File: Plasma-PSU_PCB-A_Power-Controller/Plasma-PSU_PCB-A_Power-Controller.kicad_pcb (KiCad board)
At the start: 2 copper layers, 160 x 100 mm, 98 parts, among them J201 PWR_FWD, J202 PWM_FWD, J203 Molex Mini-fit Jr. 39-28-1243, J204 Molex Mini-fit Jr. 39-28-1083, J205 Molex Mini-fit Jr. 39-28-1083, J206 Pinheader Controls, J207 ENBL_FWD, J301 Arduino_Pinout_01-15, J302 SPI, J303 UART, J304 I2C, J305 Arduino_Pinout_16-30, J501 Probe_Vin, J502 Probe_Iin, J503 JP_RUN, J504 Probe_Iout, J505 Probe_Vout, J506 Probe_DAC_A, J507 Probe_DAC_B, J508 OPAMP_Vout, J509 OPAMP_Iout, Q201 BC818, Q202 BC818, Q203 BT169B, Q204 BC808, Q501 NVTFS6H850NL, Q502 NVTFS6H850NL, U201 STM6600, U501 MCP602, U502 MCP602, U503 LTC3786, U504 MCP4822

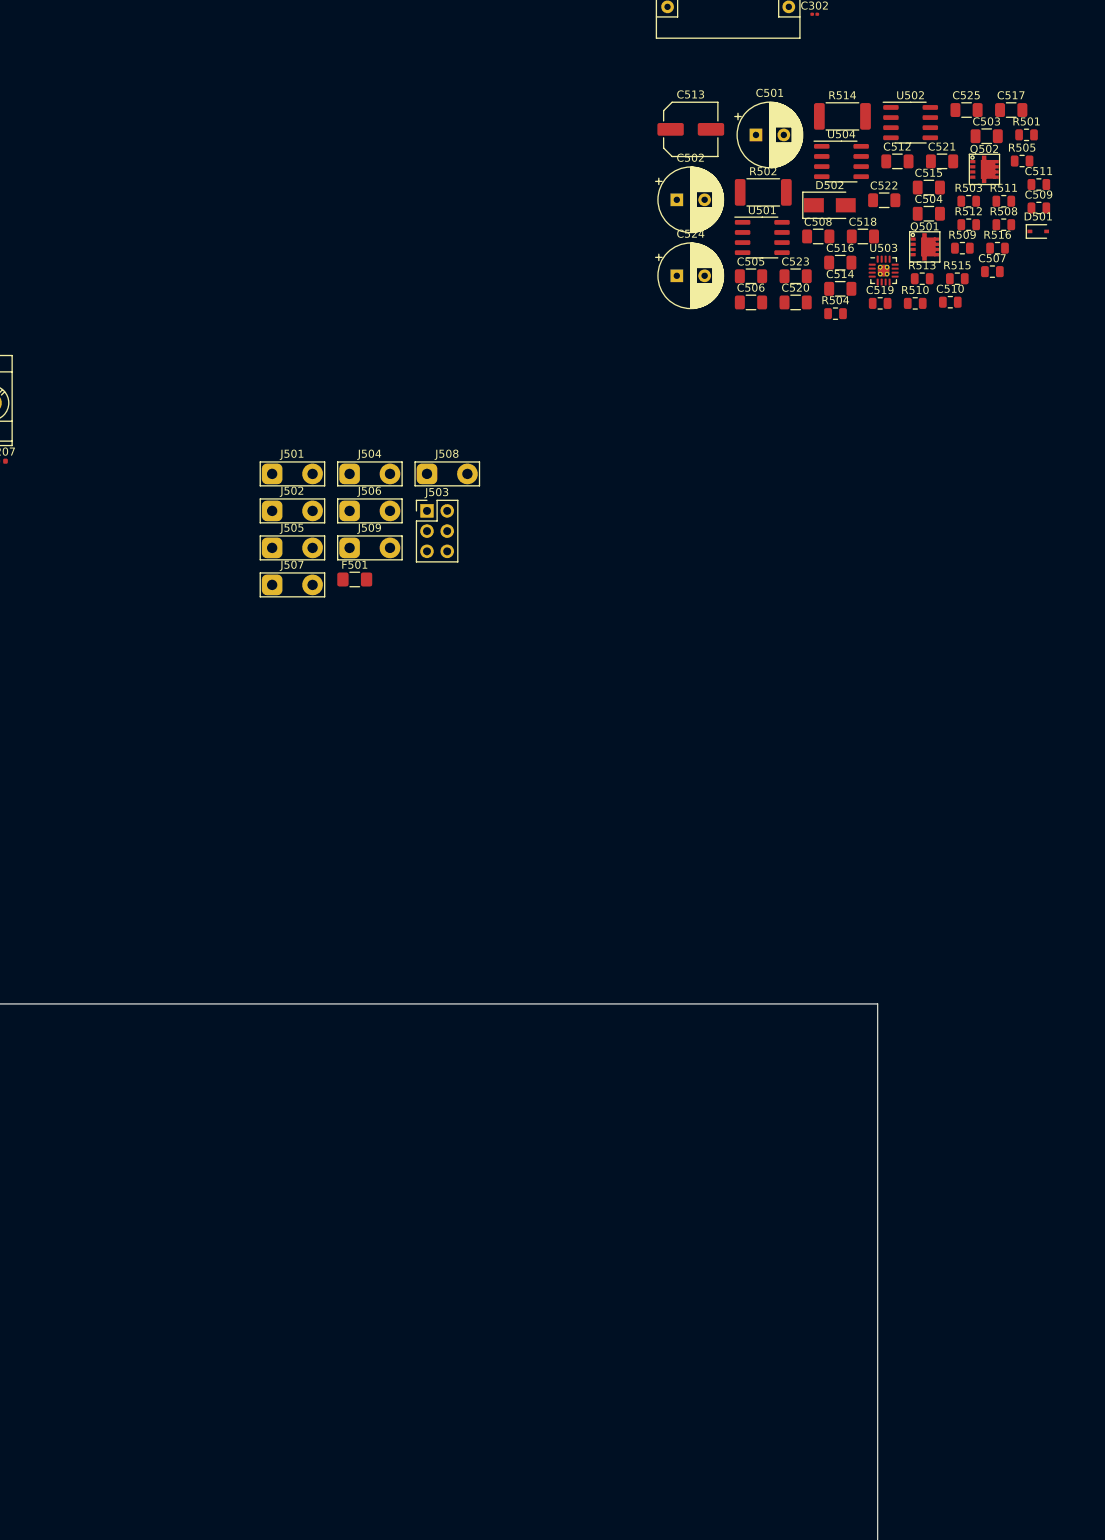
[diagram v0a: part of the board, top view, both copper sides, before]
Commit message: Power Inductor updated
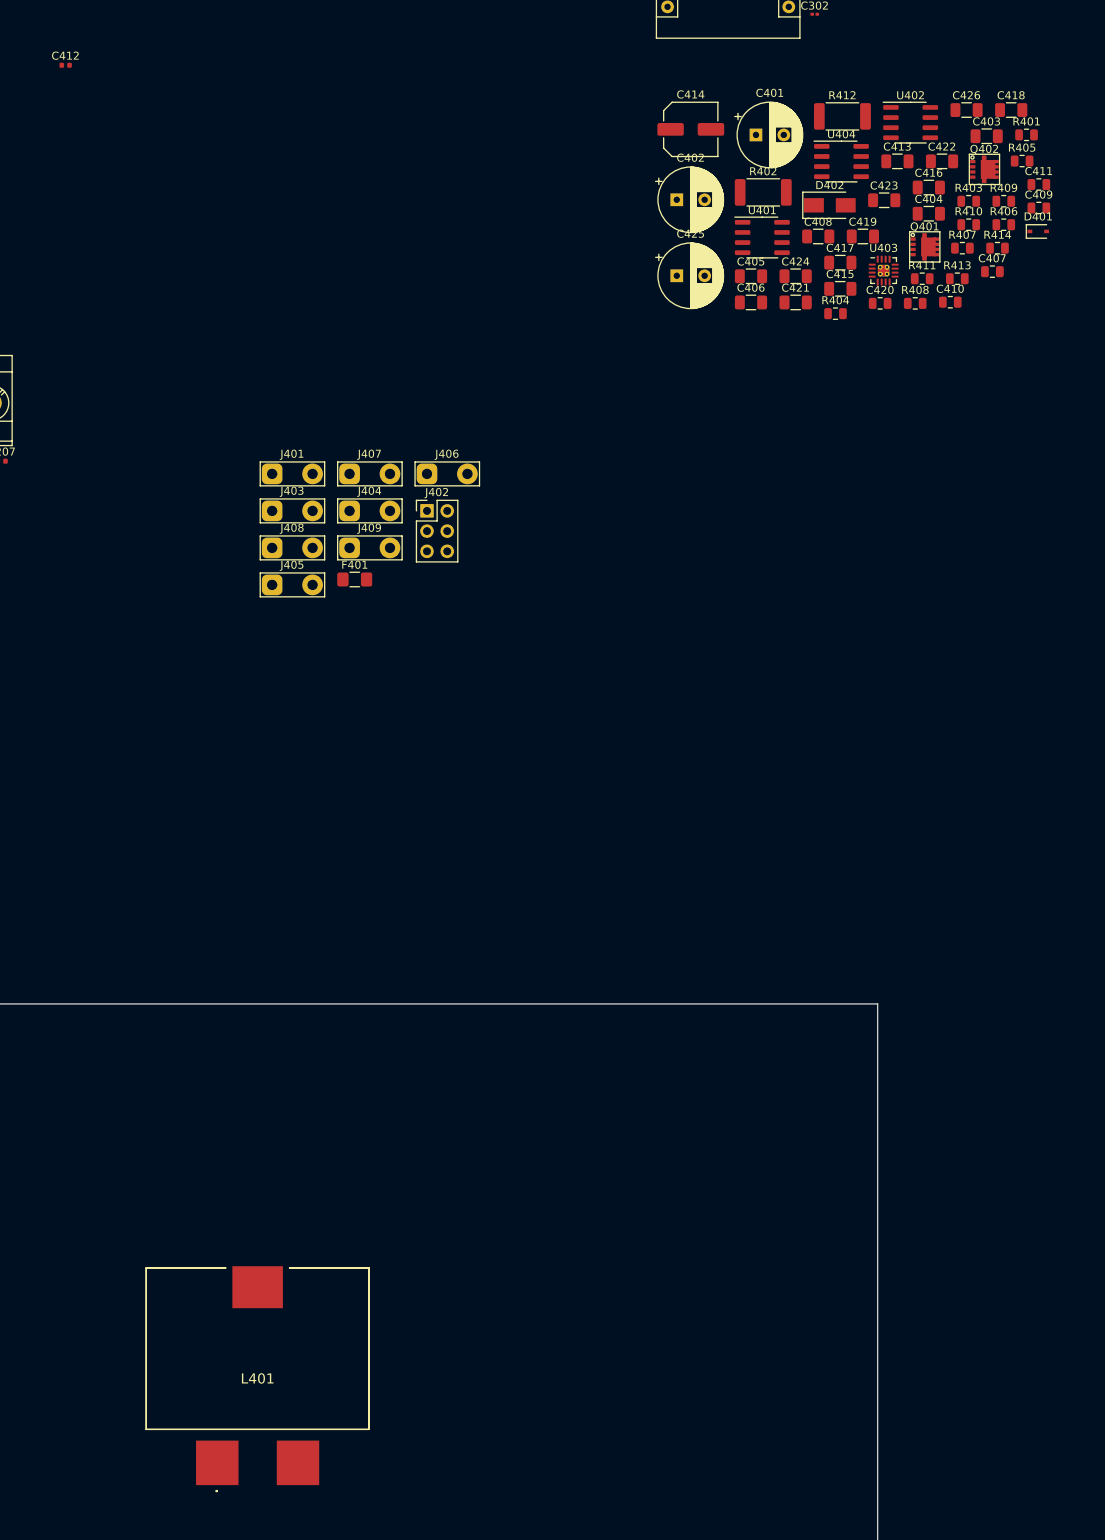
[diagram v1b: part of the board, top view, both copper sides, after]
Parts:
- added C412: 100pF, Capacitor_SMD:C_0402_1005Metric, F.Cu at (121.9, -81.3)
- added L401: 7443640330B, SamacSys_PCB_library:7443640330B, F.Cu at (146.1, 80.0)
- R402: renamed from R502; value 2mR -> 1.1mR
- renumbered C501 to C401, C502 to C402, C503 to C403, C504 to C404, C505 to C405, C506 to C406, C507 to C407, C508 to C408, C509 to C409, C510 to C410, C511 to C411, C512 to C413, C513 to C414, C514 to C415, C515 to C416, C516 to C417, C517 to C418, C518 to C419, C519 to C420, C520 to C421, C521 to C422, C522 to C423, C523 to C424, C524 to C425, C525 to C426, D501 to D401, D502 to D402, F501 to F401, J501 to J401, J503 to J402, J502 to J403, J506 to J404, J507 to J405, J508 to J406, J504 to J407, J505 to J408, J509 to J409, Q501 to Q401, Q502 to Q402, R501 to R401, R503 to R403, R504 to R404, R505 to R405, R508 to R406, R509 to R407, R510 to R408, R511 to R409, R512 to R410, R513 to R411, R514 to R412, R515 to R413, R516 to R414, U501 to U401, U502 to U402, U503 to U403, U504 to U404
